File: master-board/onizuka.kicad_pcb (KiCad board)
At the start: 2 copper layers, 27.5 x 20.5 mm, 29 parts, among them IC1 FT232RQ, IC2 ADCMP371, P1 USB_OTG, P2 FTDI, Q1 Q_PMOS_DGS, SW1 SWITCH_INV, U1 LD1117S33TR

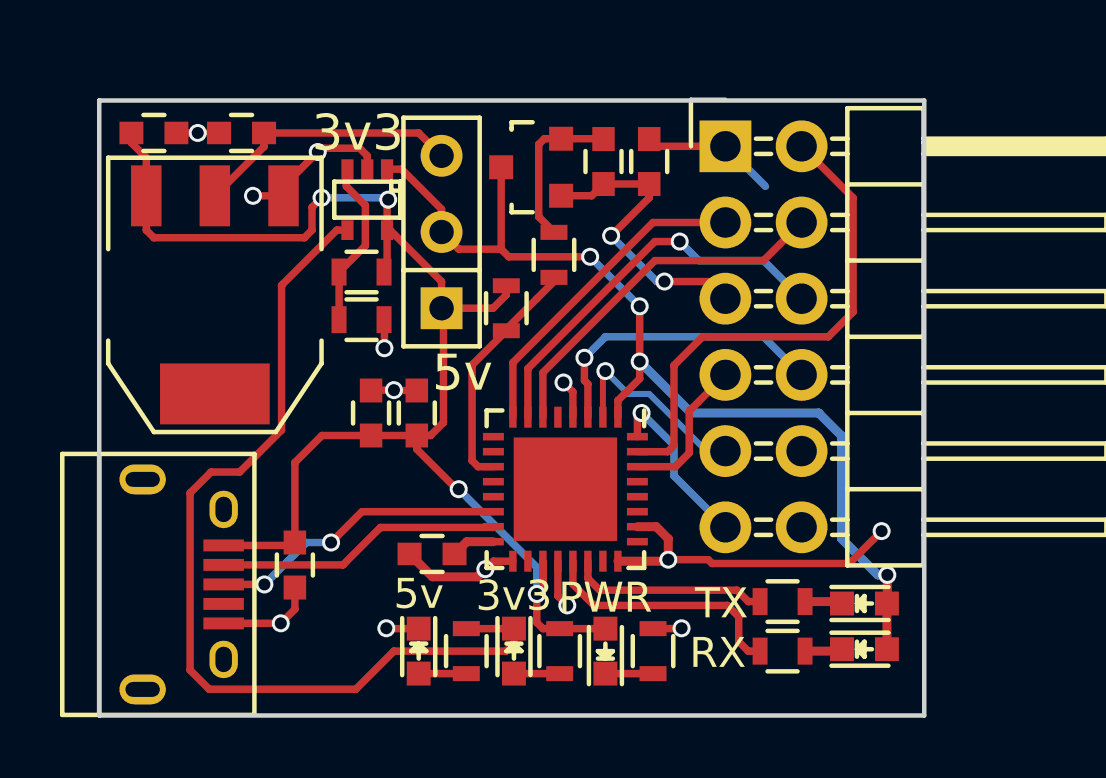
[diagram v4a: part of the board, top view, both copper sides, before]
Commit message: Board reshuffle, new regulator
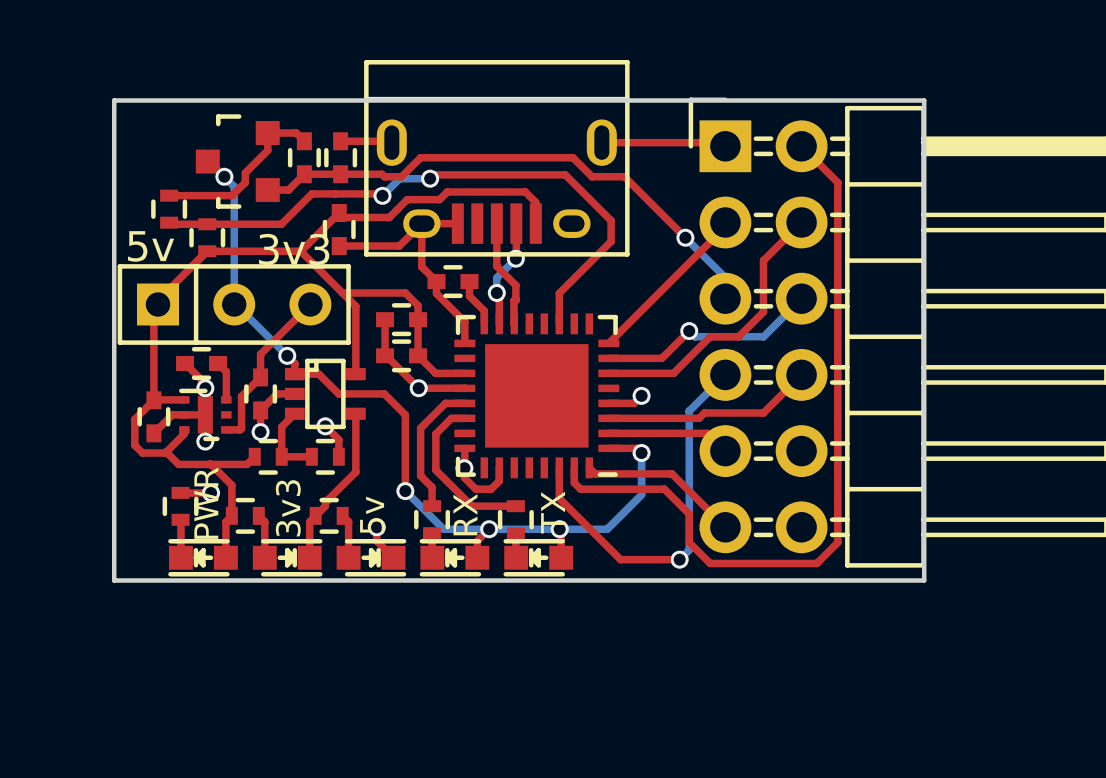
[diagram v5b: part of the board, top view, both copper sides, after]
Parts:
- added C9: 1u, Capacitors_SMD:C_0402, F.Cu at (45.9, 28.8)
- C1, C2, C3, C4, C5, C6: footprint Capacitors_SMD:C_0603 -> Capacitors_SMD:C_0402
- C7: value 100n -> 1u; footprint Capacitors_SMD:C_0603 -> Capacitors_SMD:C_0402
- C8: value 10u -> 1u; footprint Capacitors_SMD:C_0603 -> Capacitors_SMD:C_0402
- R1, R2, R3, R4, R5, R6, R7, R8, R9: footprint Resistors_SMD:R_0603 -> Resistors_SMD:R_0402
- U1: value LD1117S33TR -> MIC5353-3.3YMT; footprint SOT-223 -> Housings_MLF:Thin_MLF_6_1.6mm_0.5mm_pitch
- moved P1 17.3 mm to (55.8, 22.5), turned to 180 degrees
- moved R3 16.5 mm to (45.2, 33.5)
- moved D2 14.0 mm to (54.4, 35.2)
- moved D3 13.8 mm to (46.0, 35.2), turned to 0 degrees
- moved R4 12.9 mm to (44.8, 23.6)
- moved R2 12.5 mm to (53.6, 34.0), turned to 90 degrees
- moved R7 11.4 mm to (47.4, 33.8), turned to 0 degrees
- moved C2 11.3 mm to (50.5, 24.3)
- moved D1 11.0 mm to (57.1, 35.2)
- moved C6 10.3 mm to (50.5, 21.9)
- moved R9 10.2 mm to (46.1, 24.6), turned to 90 degrees
- moved C5 9.97 mm to (49.3, 21.9)
- moved Q1 9.78 mm to (47.1, 22.0)
- moved C7 9.46 mm to (44.3, 30.5), turned to 270 degrees
- moved R1 9.30 mm to (56.4, 34.0), turned to 90 degrees
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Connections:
- U1 pad 1: GND -> +5V
- U1 pad 2: +3V3 -> GND
- U1 pad 4: (no net) -> +3V3
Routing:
- net /LEDCTRL: track 31.4 -> 5.47 mm
- net /PWREN: track 8.03 -> 20.3 mm, vias 0 -> 2
- net /PWROUT: track 10.0 -> 18.1 mm, vias 2 -> 1
- net /DTR: track 16.9 -> 25.0 mm
- net /TXD: track 5.02 -> 13.0 mm, vias 0 -> 1
- net /USBD+: track 10.00 -> 3.67 mm, vias 2 -> 0
- net +5V: track 48.0 -> 42.1 mm, vias 4 -> 0
- net /USBD-: track 9.53 -> 3.64 mm, vias 0 -> 2
- net /DCD: track 13.3 -> 7.41 mm
- net /CTS: track 10.8 -> 5.64 mm
- net /VCCIO: track 33.3 -> 28.7 mm, vias 4 -> 6
- net /RXLED: track 8.42 -> 4.57 mm
- net +3V3: track 9.01 -> 5.61 mm
- net /RI: track 10.1 -> 7.03 mm, vias 1 -> 0
- net /4v5: track 5.66 -> 2.62 mm
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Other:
- board size 27.5 x 20.5 mm -> 27 x 16 mm

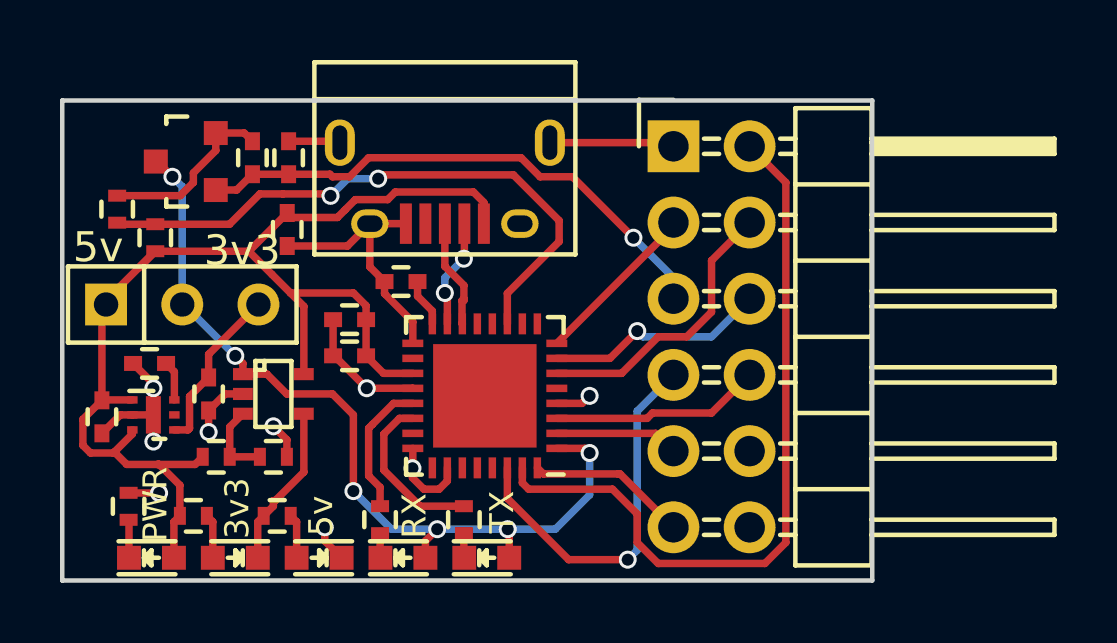
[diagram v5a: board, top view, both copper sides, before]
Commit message: Faffing, added connections to heatsink pad on FTDI, moved connector in slightly.
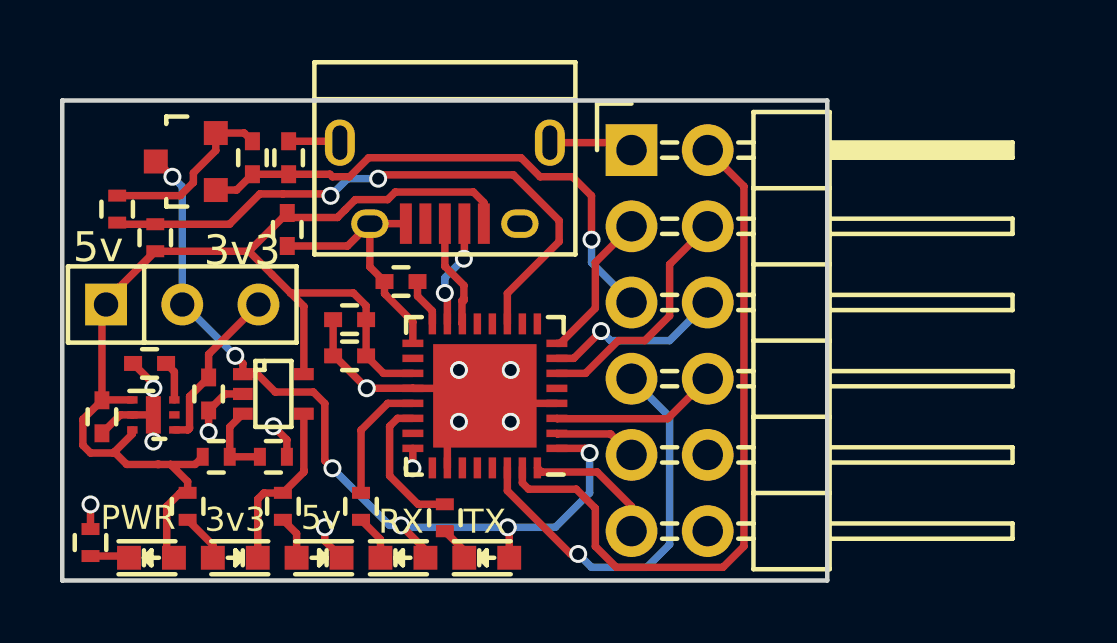
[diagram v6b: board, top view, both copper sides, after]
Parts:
- moved R3 1.75 mm to (43.9, 34.7)
- moved P2 1.40 mm to (62.0, 21.7)
- moved R2 0.78 mm to (53.0, 33.5)
- moved R1 0.64 mm to (55.8, 33.9)
- moved R7 0.37 mm to (47.2, 33.5), turned to 270 degrees
- moved R8 0.37 mm to (50.4, 33.5), turned to 270 degrees
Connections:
- IC1 pad 33: (no net) -> GND
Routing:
- net /DSR: track 9.51 -> 8.06 mm
- net /RI: track 7.03 -> 5.59 mm
- net /RXD: track 4.13 -> 2.79 mm
- net /DCD: track 7.41 -> 6.06 mm
- net /DTR: track 25.0 -> 23.8 mm
- net /RTS: track 5.36 -> 4.50 mm
- net /TXLED: track 5.55 -> 4.77 mm
- net Net-(D2-Pad1): track 0.83 -> 1.55 mm
- net /CTS: track 5.64 -> 5.00 mm
- net /TXD: track 13.0 -> 13.6 mm
- net GND: track 34.4 -> 34.8 mm, vias 9 -> 12
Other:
- board size 27 x 16 mm -> 25.5 x 16 mm

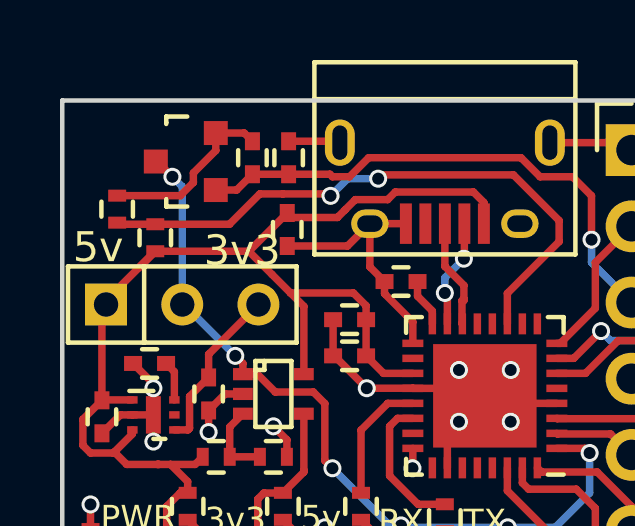
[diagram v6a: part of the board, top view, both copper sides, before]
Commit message: Tidied up schema, started to add farnell codes for components.
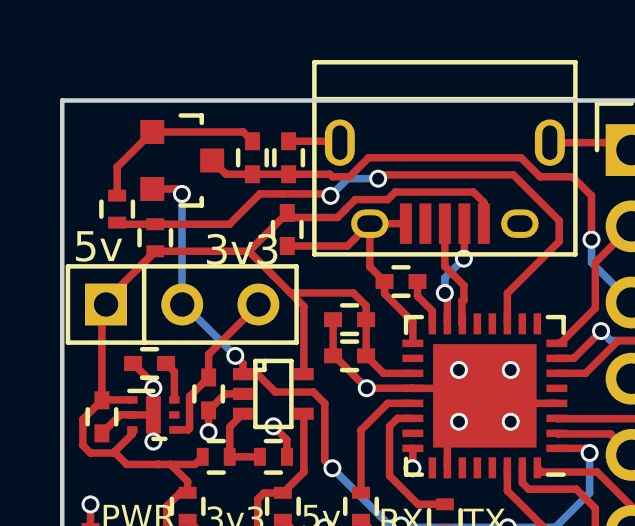
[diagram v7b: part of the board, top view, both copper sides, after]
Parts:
- Q1: value Q_PMOS_DGS -> Q_PMOS_GSD
- moved Q1 0.12 mm to (47.0, 22.0), turned to 270 degrees
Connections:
- net /4v5 renamed +4v5
- Q1 pad 1: /PWROUT -> Net-(C5-Pad2)
- Q1 pad 2: Net-(C5-Pad2) -> /VCCIO
- Q1 pad 3: /VCCIO -> /PWROUT

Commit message: Various tweaks
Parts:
- C3: value 4.7u -> 4u7
- IC1: footprint Housings_DFN_QFN:QFN-32-1EP_5x5mm_Pitch0.5mm -> ftdi:FTDI-FT232RQ-QFN-32
- R1, R2, R3: value 270R -> 1k
- R4: value 1k -> 1K
- R5: value 510K -> 51K
- R6: value 4M3 -> 430K
- R7, R8: value 680R -> 1k
- R9: value 10k -> 10K
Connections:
- net +4v5 renamed Net-(IC2-Pad3)
- IC1 pad 10: Net-(IC1-Pad10) -> (no net)
- IC1 pad 12: Net-(IC1-Pad12) -> (no net)
- IC1 pad 13: Net-(IC1-Pad13) -> (no net)
- IC1 pad 18: Net-(IC1-Pad18) -> (no net)
- IC1 pad 23: Net-(IC1-Pad23) -> (no net)
- IC1 pad 25: Net-(IC1-Pad25) -> (no net)
- IC1 pad 27: Net-(IC1-Pad27) -> (no net)
- IC1 pad 28: Net-(IC1-Pad28) -> (no net)
- IC1 pad 29: Net-(IC1-Pad29) -> (no net)
- IC1 pad 5: Net-(IC1-Pad5) -> (no net)
- IC1 pad 9: Net-(IC1-Pad9) -> (no net)
- P1 pad 4: Net-(P1-Pad4) -> (no net)
- P2 pad 10: Net-(P2-Pad10) -> (no net)
- P2 pad 12: Net-(P2-Pad12) -> (no net)
- U1 pad 5: Net-(U1-Pad5) -> (no net)
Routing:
- net GND: track 34.8 -> 39.1 mm
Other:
- rule pad_to_mask_clearance: 0.2 -> 0
